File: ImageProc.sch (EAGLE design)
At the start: 119 parts, among them IC1 XC61GC3002HR-G, IC10 AT45DB642D-CNU, IC2 MIC5335-SPYMT, IC3 MIC5335-JGYMT, IC4 DSPIC33FJ128MC706A, IC5 AT86RF233-ZU, IC6 LTC6088, IC7 DRV8833RTY, IC8 DRV8833RTY, IC9 MPU-6000, P1 BAT+, P10 MD2, P11 EXT1, P12 EXT2, P13 EXT3, P14 EXT4, P16 EXT5, P2 BAT-, P3 MA1, P4 MA2, P5 MB1, P6 MB2, P7 MC1, P8 MC2, P9 MD1

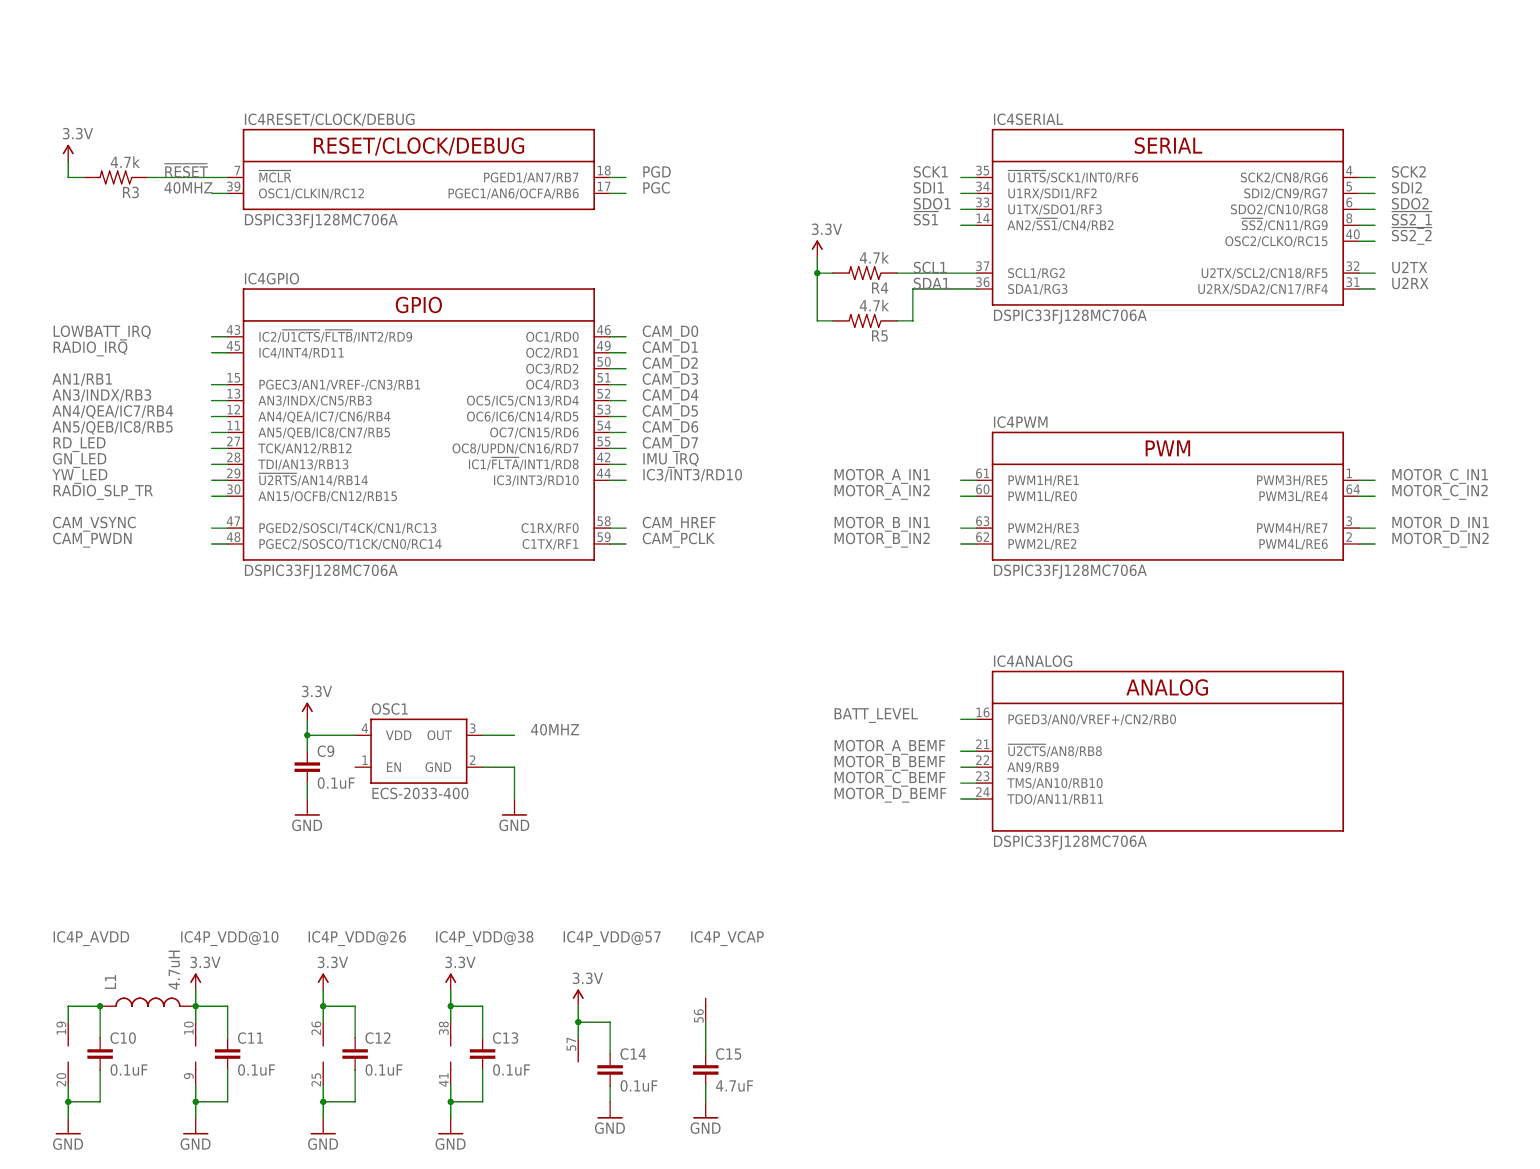
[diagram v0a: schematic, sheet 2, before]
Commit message: Initial strip of the IP2.5 Rev C board. dsPic and camera connector removed.
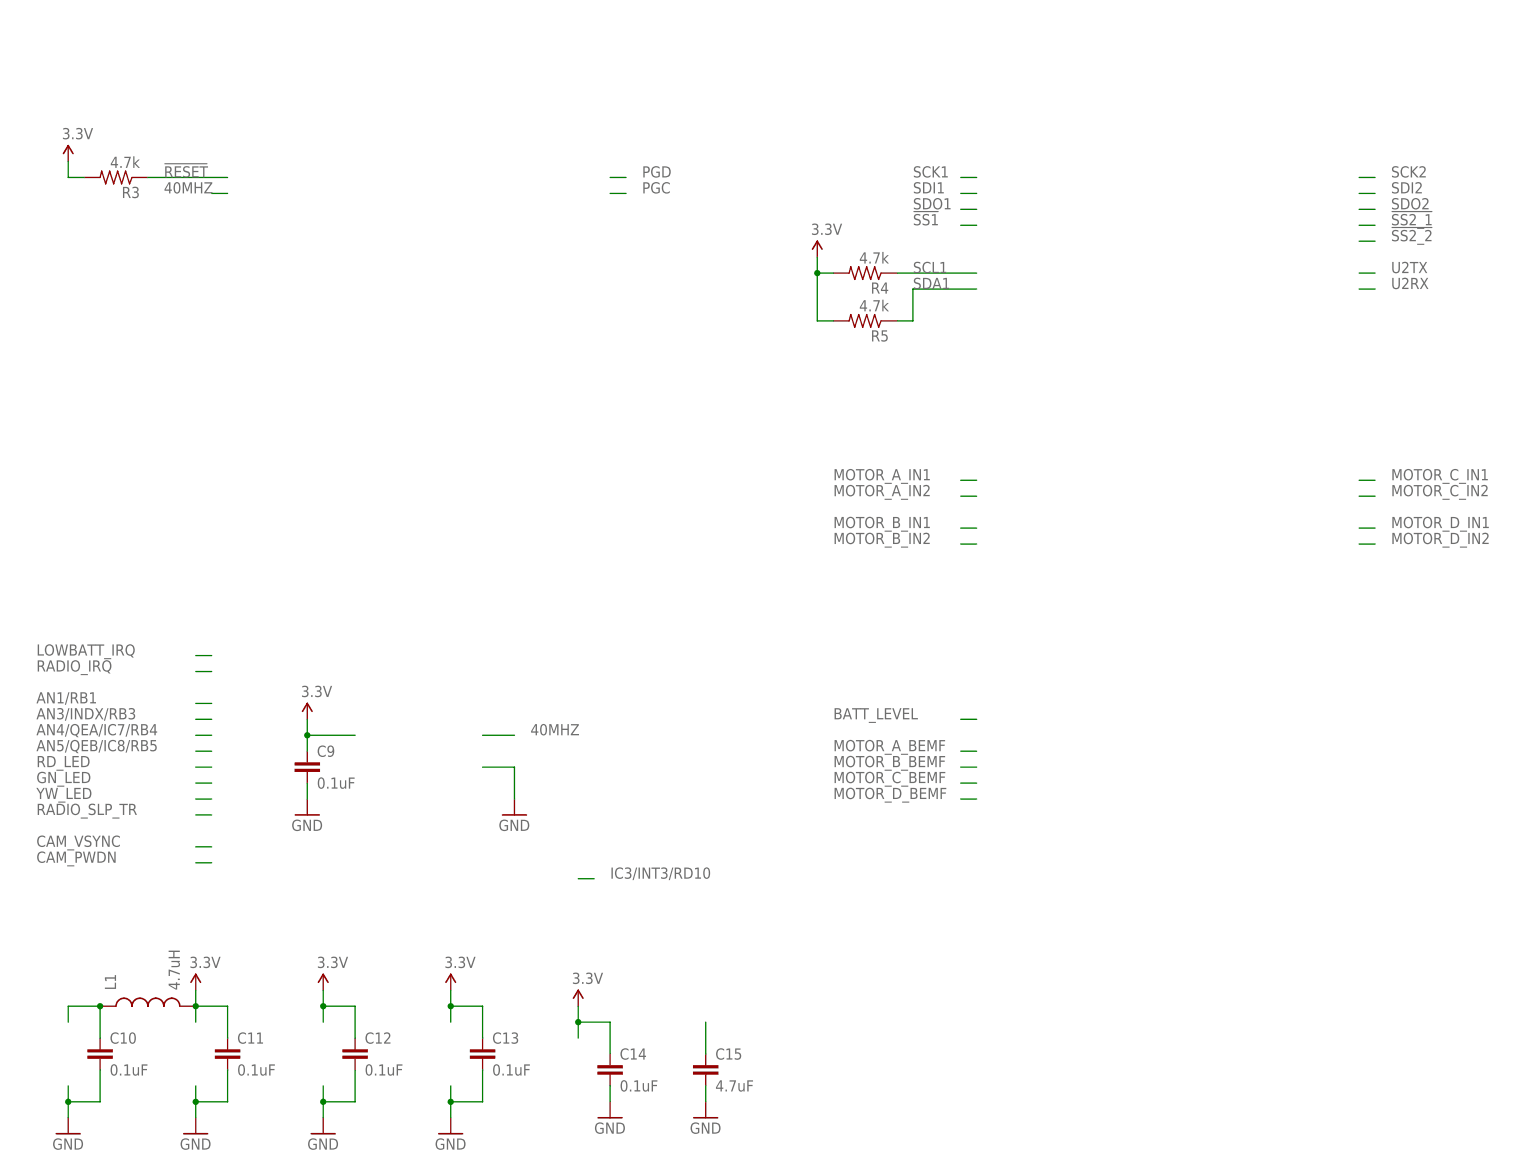
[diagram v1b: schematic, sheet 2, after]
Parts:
- removed C36: 0.1uF, biomimetic:CAP0402-CAP
- removed IC4: DSPIC33FJ128MC706A, biomimetic:DSPIC33FJ128MC706A
- removed JP4: 51441-2493-C, biomimetic:OV7660FSL_CON
- removed OSC1: ECS-2033-400, biomimetic:ECS-2033-400
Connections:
- removed net 40MHZ: IC4RESET/CLOCK/DEBUG.OSC1/CLKIN/RC12, JP4.XCLK, OSC1.OUT
- removed net CAM_D0: IC4GPIO.OC1/RD0, JP4.D0
- removed net CAM_D1: IC4GPIO.OC2/RD1, JP4.D1
- removed net CAM_D2: IC4GPIO.OC3/RD2, JP4.D2
- removed net CAM_D3: IC4GPIO.OC4/RD3, JP4.D3
- removed net CAM_D4: IC4GPIO.OC5/IC5/CN13/RD4, JP4.D4
- removed net CAM_D5: IC4GPIO.OC6/IC6/CN14/RD5, JP4.D5
- removed net CAM_D6: IC4GPIO.OC7/CN15/RD6, JP4.D6
- removed net CAM_D7: IC4GPIO.OC8/UPDN/CN16/RD7, JP4.D7
- removed net CAM_PCLK: IC4GPIO.C1TX/RF1, JP4.PCLK
- removed net CAM_PWDN: IC4GPIO.PGEC2/SOSCO/T1CK/CN0/RC14, JP4.PWDN
- removed net CAM_VSYNC: IC4GPIO.PGED2/SOSCI/T4CK/CN1/RC13, JP4.VSYNC
- net !RESET: no longer IC4RESET/CLOCK/DEBUG.!MCLR
- net !SS1: no longer IC4SERIAL.AN2/!SS1!/CN4/RB2
- net !SS2_1: no longer IC4SERIAL.!SS2!/CN11/RG9
- net !SS2_2: no longer IC4SERIAL.OSC2/CLKO/RC15
- net 1.8V: no longer JP4.DVDD
- net 2.5V: no longer C36.2, JP4.AVDD, JP4.DOVDD
- net 3.3V: no longer IC4P_VDD@10.V+, IC4P_VDD@26.V+, IC4P_VDD@38.V+, IC4P_VDD@57.V+, OSC1.VDD
- net AN1/RB1: no longer IC4GPIO.PGEC3/AN1/VREF-/CN3/RB1
- net AN3/INDX/RB3: no longer IC4GPIO.AN3/INDX/CN5/RB3
- net AN4/QEA/IC7/RB4: no longer IC4GPIO.AN4/QEA/IC7/CN6/RB4
- net AN5/QEB/IC8/RB5: no longer IC4GPIO.AN5/QEB/IC8/CN7/RB5
- net BATT_LEVEL: no longer IC4ANALOG.PGED3/AN0/VREF+/CN2/RB0
- net CAM_HREF: no longer IC4GPIO.C1RX/RF0, JP4.HREF
- net GND: no longer C36.1, IC4P_AVDD.V-, IC4P_VDD@10.V-, IC4P_VDD@26.V-, IC4P_VDD@38.V-, JP4.AGND, JP4.DGND, JP4.RESET, OSC1.GND
- net GN_LED: no longer IC4GPIO.TDI/AN13/RB13
- net IC3/INT3/RD10: no longer IC4GPIO.IC3/INT3/RD10
- net IMU_IRQ: no longer IC4GPIO.IC1/!FLTA!/INT1/RD8
- net LOWBATT_IRQ: no longer IC4GPIO.IC2/!U1CTS!/!FLTB!/INT2/RD9
- net MOTOR_A_BEMF: no longer IC4ANALOG.!U2CTS!/AN8/RB8
- net MOTOR_A_IN1: no longer IC4PWM.PWM1H/RE1
- net MOTOR_A_IN2: no longer IC4PWM.PWM1L/RE0
- net MOTOR_B_BEMF: no longer IC4ANALOG.AN9/RB9
- net MOTOR_B_IN1: no longer IC4PWM.PWM2H/RE3
- net MOTOR_B_IN2: no longer IC4PWM.PWM2L/RE2
- net MOTOR_C_BEMF: no longer IC4ANALOG.TMS/AN10/RB10
- net MOTOR_C_IN1: no longer IC4PWM.PWM3H/RE5
- net MOTOR_C_IN2: no longer IC4PWM.PWM3L/RE4
- net MOTOR_D_BEMF: no longer IC4ANALOG.TDO/AN11/RB11
- net MOTOR_D_IN1: no longer IC4PWM.PWM4H/RE7
- net MOTOR_D_IN2: no longer IC4PWM.PWM4L/RE6
- net N$21: no longer IC4P_AVDD.V+
- net N$28: no longer IC4P_VCAP.V+
- net PGC: no longer IC4RESET/CLOCK/DEBUG.PGEC1/AN6/OCFA/RB6
- net PGD: no longer IC4RESET/CLOCK/DEBUG.PGED1/AN7/RB7
- net RADIO_IRQ: no longer IC4GPIO.IC4/INT4/RD11
- net RADIO_SLP_TR: no longer IC4GPIO.AN15/OCFB/CN12/RB15
- net RD_LED: no longer IC4GPIO.TCK/AN12/RB12
- net SCK1: no longer IC4SERIAL.!U1RTS!/SCK1/INT0/RF6
- net SCK2: no longer IC4SERIAL.SCK2/CN8/RG6
- net SCL1: no longer IC4SERIAL.SCL1/RG2, JP4.SIO_C
- net SDA1: no longer IC4SERIAL.SDA1/RG3, JP4.SIO_D
- net SDI1: no longer IC4SERIAL.U1RX/SDI1/RF2
- net SDI2: no longer IC4SERIAL.SDI2/CN9/RG7
- net SDO1: no longer IC4SERIAL.U1TX/SDO1/RF3
- net SDO2: no longer IC4SERIAL.SDO2/CN10/RG8
- net U2RX: no longer IC4SERIAL.U2RX/SDA2/CN17/RF4
- net U2TX: no longer IC4SERIAL.U2TX/SCL2/CN18/RF5
- net YW_LED: no longer IC4GPIO.!U2RTS!/AN14/RB14

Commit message: Initial placement of part with fixed functon pins in place, other pins as placeholders. Library part now active.
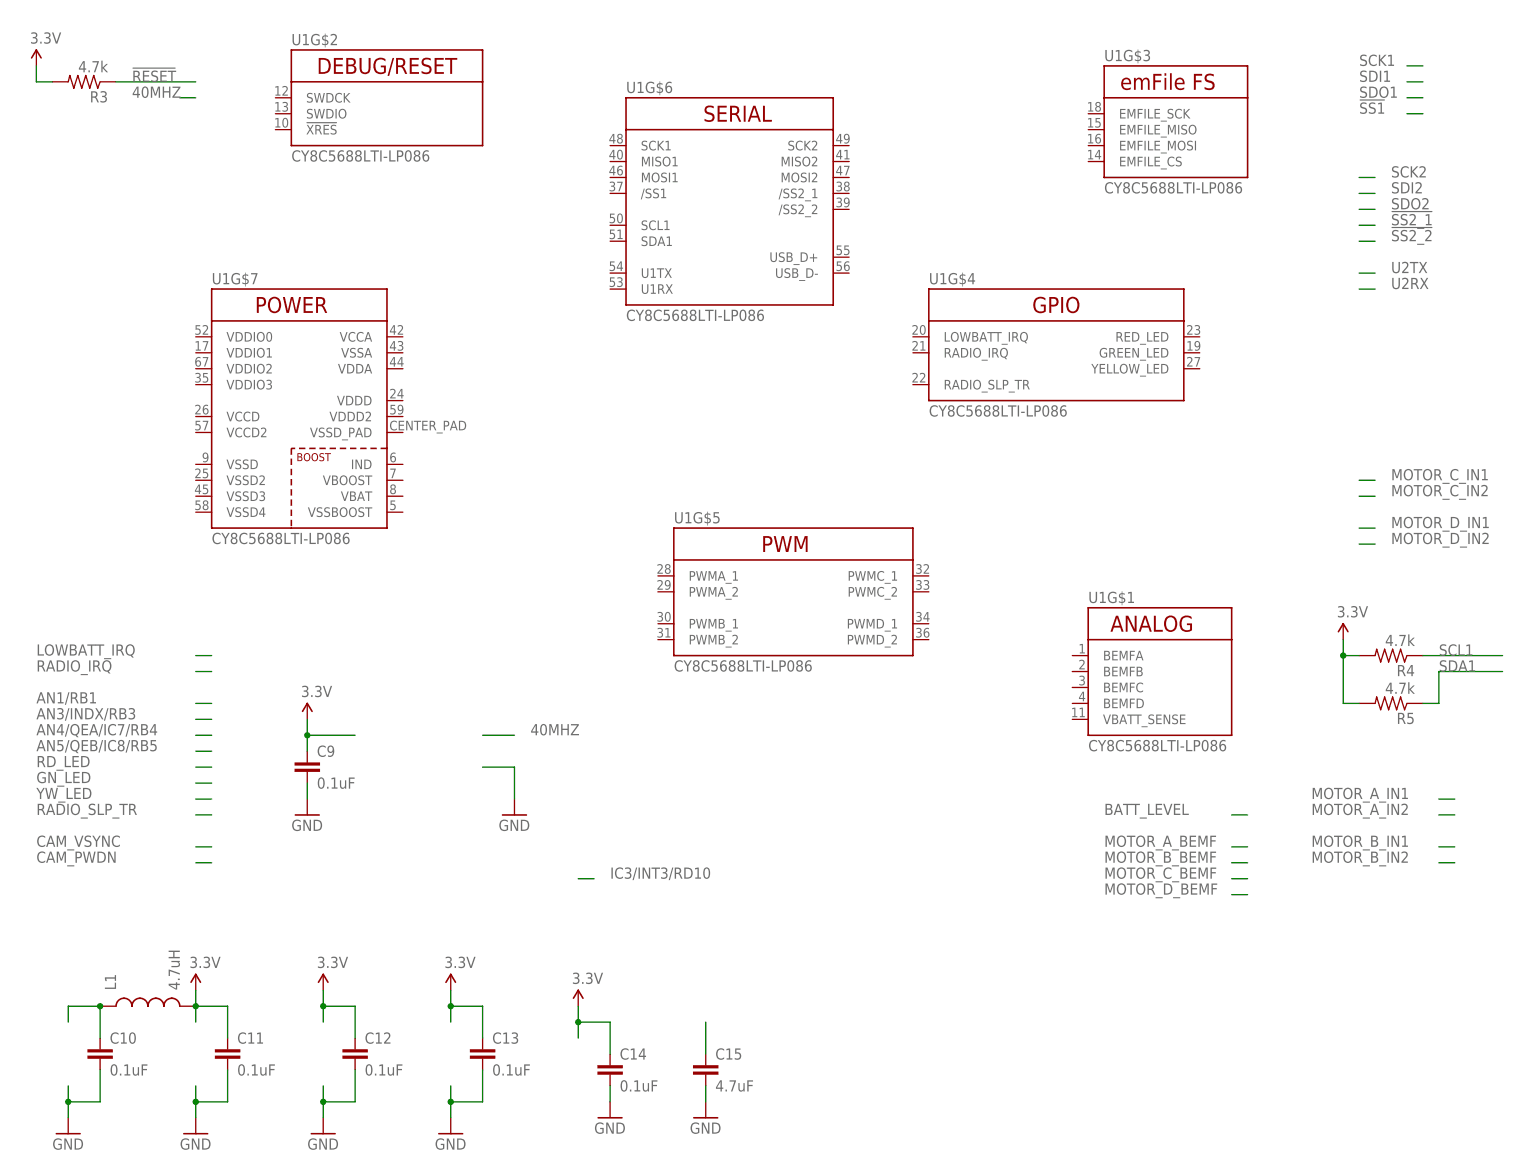
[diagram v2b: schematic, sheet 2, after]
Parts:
- removed PWM1, PWM2: EXT5, wirepad:SMD2
- added U1: CY8C5688LTI-LP086, pullin:CY8C5688LTI-LP086
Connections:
- net MOTOR_C_IN2: no longer PWM1.P
- net MOTOR_D_IN2: no longer PWM2.P
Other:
- moved on the sheet: R3, R4, R5
